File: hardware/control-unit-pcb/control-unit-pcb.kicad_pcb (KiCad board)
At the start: 2 copper layers, 17.8 x 43.2 mm, 6 parts, among them P1 Digital, P2 Analog, P3 CONN_01X01, P4 CONN_01X01, P5 CONN_01X01, P6 CONN_01X01

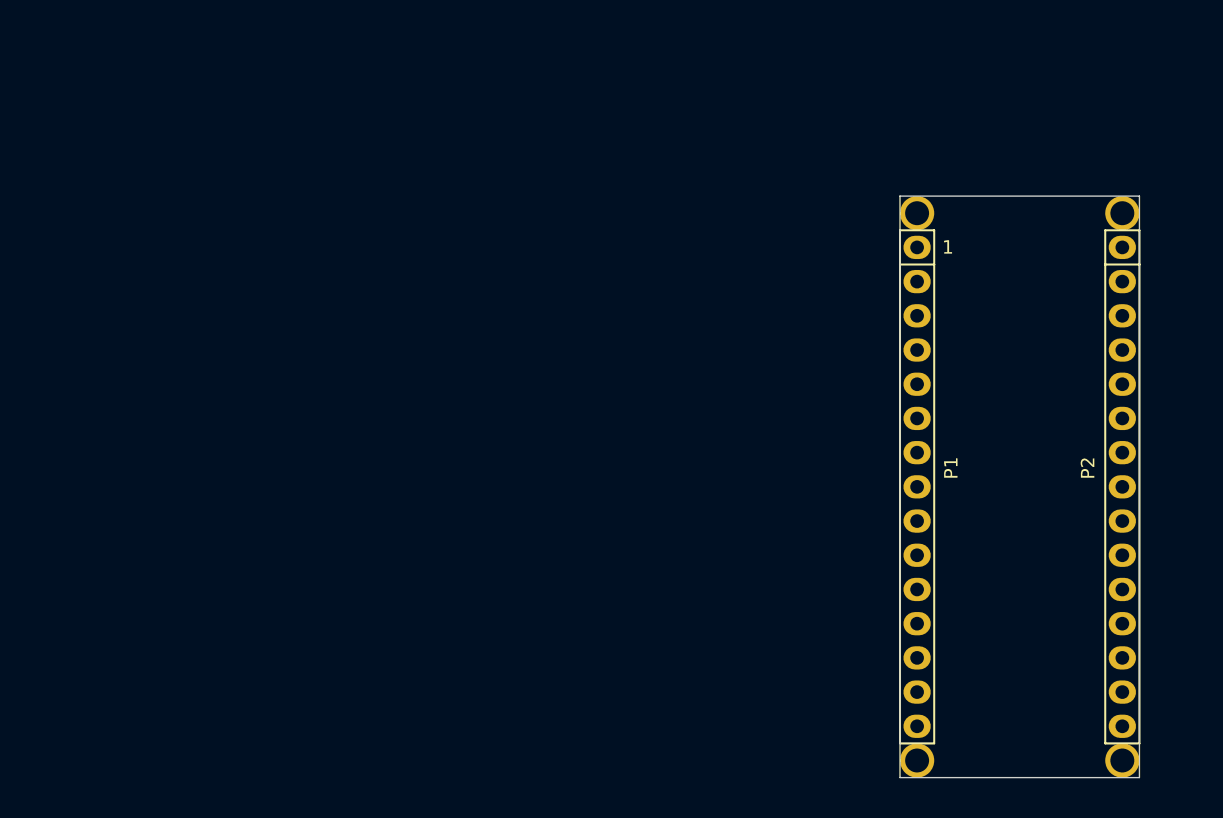
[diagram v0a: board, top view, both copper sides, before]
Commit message: Update ctrl module schema
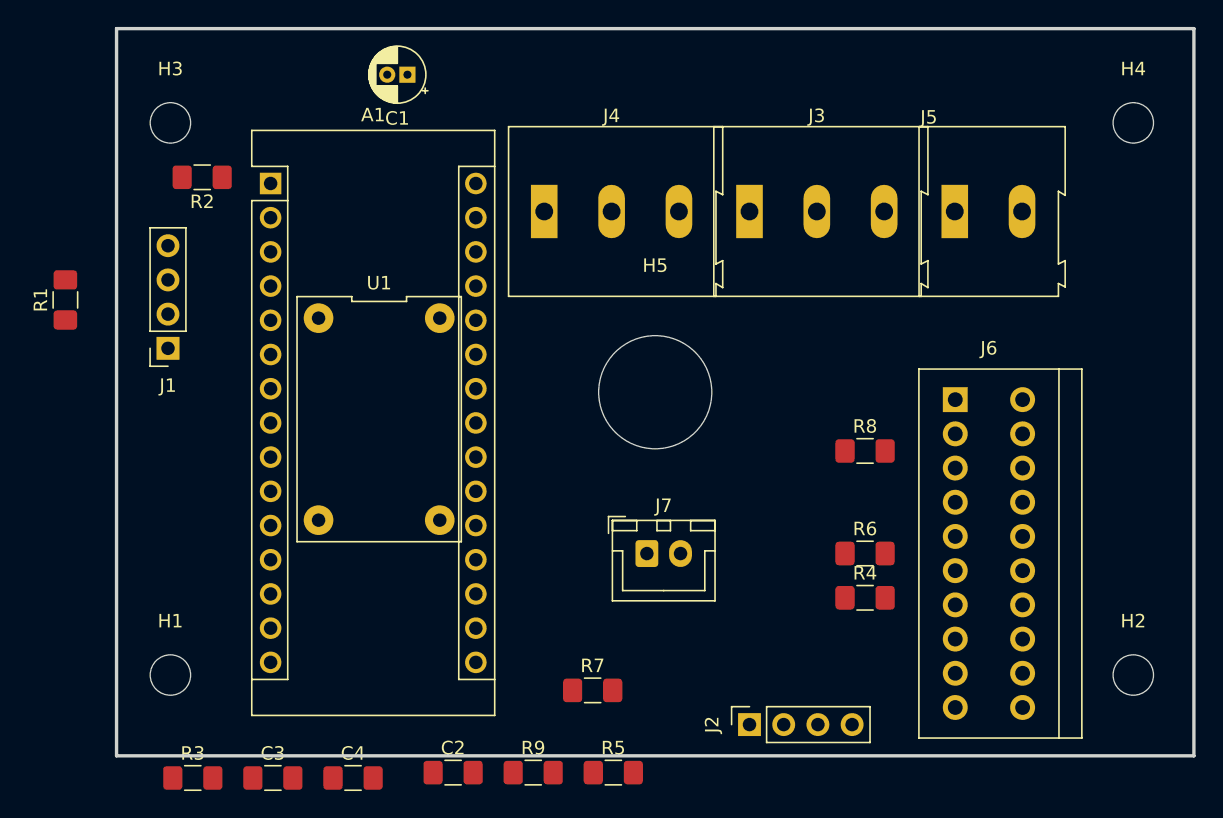
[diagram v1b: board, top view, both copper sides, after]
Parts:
- removed P1: Digital, Socket_Arduino_Nano:Socket_Strip_Arduino_1x15
- removed P2: Analog, Socket_Arduino_Nano:Socket_Strip_Arduino_1x15
- removed P3, P4, P5, P6: CONN_01X01, Socket_Arduino_Nano:1pin_Nano
- added A1: Arduino_Nano_v3.x, Module:Arduino_Nano, F.Cu at (91.4, 66.5)
- added C1: 1uF, Capacitor_THT:CP_Radial_D4.0mm_P1.50mm, F.Cu at (101.6, 58.4)
- added C2: 100nF, Capacitor_SMD:C_1206_3216Metric_Pad1.42x1.75mm_HandSolder, F.Cu at (105.0, 110.2)
- added C3: 100nF, Capacitor_SMD:C_1206_3216Metric_Pad1.42x1.75mm_HandSolder, F.Cu at (91.6, 110.6)
- added C4: 100nF, Capacitor_SMD:C_1206_3216Metric_Pad1.42x1.75mm_HandSolder, F.Cu at (97.6, 110.6)
- added H1: MountingHole, MountingHole:MountingHole_3mm, F.Cu at (84.0, 103.0)
- added H2: MountingHole, MountingHole:MountingHole_3mm, F.Cu at (155.5, 103.0)
- added H3: MountingHole, MountingHole:MountingHole_3mm, F.Cu at (84.0, 62.0)
- added H4: MountingHole, MountingHole:MountingHole_3mm, F.Cu at (155.5, 62.0)
- added H5: MountingHole, MountingHole:MountingHole_8.4mm_M8, F.Cu at (120.0, 82.0)
- added J1: Conn_01x04_Male, Connector_PinSocket_2.54mm:PinSocket_1x04_P2.54mm_Vertical, F.Cu at (83.8, 78.7)
- added J2: Conn_01x04_Male, Connector_PinSocket_2.54mm:PinSocket_1x04_P2.54mm_Vertical, F.Cu at (127.0, 106.7)
- added J3: Screw_Terminal_01x03, TerminalBlock:TerminalBlock_Altech_AK300-3_P5.00mm, F.Cu at (127.0, 68.6)
- added J4: Screw_Terminal_01x03, TerminalBlock:TerminalBlock_Altech_AK300-3_P5.00mm, F.Cu at (111.8, 68.6)
- added J5: Screw_Terminal_01x02, TerminalBlock:TerminalBlock_Altech_AK300-2_P5.00mm, F.Cu at (142.2, 68.6)
- added J6: Conn_02x10_Row_Letter_Last, TerminalBlock_PTR:TerminalBlock_PTR_AKZ3191_10KD-2x10_2.54x5.00, F.Cu at (144.8, 94.0)
- added J7: Conn_01x02_Male, Connector_JST:JST_XH_B2B-XH-A_1x02_P2.50mm_Vertical, F.Cu at (119.4, 94.0)
- added R1: 2k2, Resistor_SMD:R_1206_3216Metric_Pad1.42x1.75mm_HandSolder, F.Cu at (76.2, 75.1)
- added R2: 1k2, Resistor_SMD:R_1206_3216Metric_Pad1.42x1.75mm_HandSolder, F.Cu at (86.4, 66.0)
- added R3: R, Resistor_SMD:R_1206_3216Metric_Pad1.42x1.75mm_HandSolder, F.Cu at (85.7, 110.6)
- added R4: R, Resistor_SMD:R_1206_3216Metric_Pad1.42x1.75mm_HandSolder, F.Cu at (135.6, 97.3)
- added R5: R, Resistor_SMD:R_1206_3216Metric_Pad1.42x1.75mm_HandSolder, F.Cu at (116.9, 110.2)
- added R6: R, Resistor_SMD:R_1206_3216Metric_Pad1.42x1.75mm_HandSolder, F.Cu at (135.6, 94.0)
- added R7: R, Resistor_SMD:R_1206_3216Metric_Pad1.42x1.75mm_HandSolder, F.Cu at (115.4, 104.1)
- added R8: 2M, Resistor_SMD:R_1206_3216Metric_Pad1.42x1.75mm_HandSolder, F.Cu at (135.6, 86.4)
- added R9: 10M, Resistor_SMD:R_1206_3216Metric_Pad1.42x1.75mm_HandSolder, F.Cu at (110.9, 110.2)
- added U1: MP2307, converter_dcdc:MP2037, F.Cu at (99.5, 84.0)
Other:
- board size 17.8 x 43.2 mm -> 80 x 54 mm
- net class high power added: clearance 0.254, trace_width 0.508, via_dia 0.6, via_drill 0.4
- board text removed: "1"
